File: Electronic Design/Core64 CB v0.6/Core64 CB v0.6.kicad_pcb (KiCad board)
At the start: 2 copper layers, 85 x 85 mm, 54 parts, among them J1 Digi-Key 77311-420-36LF-ND, J2 Digi-Key 77311-420-36LF-ND, U1 SI7210-B-01, U10 TS3A4751PWR, U11 SM353LT, U12 SM353LT, U13 SM353LT, U14 LTR-329ALS-01, U2 SI7210-B-02, U3 SI7210-B-03, U4 SI7210-B-04, U5 BH1730FVC, U6 BH1730FVC, U7 LTR-303ALS-01, U8 SM353LT, U9 TS3A4751PWR, X1 SFH11-NBPC-D03-ST-BK

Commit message: CB refine silkscreen, change center ALS BH1730 opening to drill hole and remove center solder pad, clean-up ref. des. numbers
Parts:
- J1, J2: value Digi-Key 77311-420-36LF-ND -> 929834-04-36-RK
- renumbered C7 to C6, C8 to C7, C9 to C8, R7 to R5, R5 to R6, U11 to U10, U12 to U11, U13 to U12, U9 to U13, U10 to U14, U14 to U8, U8 to U9
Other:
- outline, holes or cut-outs redrawn
- board text added: "*5V0 *GND XT3,7 XT2,6 XT1,5 XT0,4 XB0 XB1 XB2 XB3 XB4 XB5 XB6 XB7 P1G1 P2G2 CP3 CP4 *+BAT *5USB"
- board text added: "*LSIG *USR1 YL0 YL1 YL2 YL3 YL4,6 YL5,7 SEN2 SEN1 SCL SDA 3V3 GNDD CP8 CP7 CP6 CP5 *USR2 *USR3"
- board text added: "*Pass-through, not connected to Core Board"
- board text added: "5V0* GND* XT3,7 XT2,6 XT1,5 XT0,4 XB0 XB1 XB2 XB3 XB4 XB5 XB6 XB7 P1G1 P2G2 CP3 CP4 +BATT* 5VUSB*"
- board text added: "ANDY GEPPERT"
- board text added: "BOTTOM SIDE"
- board text added: "CORE BOARD (CB) PCB P/N: 122-001 V0.6 (2021-08-08)"
- board text added: "LSIG* USR1* YL0 YL1 YL2 YL3 YL4,6 YL5,7 SEN2 SEN1 SCL SDA 3V3 GNDD CP8 CP7 CP6 CP5 USR2* USR3*"
- board text added: "TOP SIDE"
- board text added: "WWW.MACHINEIDEAS.COM"
- board text removed: "5V0 GND XT3,7 XT2,6 XT1,5 XT0,4 XB0 XB1 XB2 XB3 XB4 XB5 XB6 XB7 P1G1 P2G2 CP3 CP4 +BATT 5VUSB"
- board text removed: "CORE BOARD V0.6 2021-06-07 ANDY GEPPERT WWW.MACHINEIDEAS.COM"
- board text removed: "LSIG USR1 YL0 YL1 YL2 YL3 YL4,6 YL5,7 SEN2 SEN1 SCL SDA 3V3 GNDD CP8 CP7 CP6 CP5 USR2 USR3"

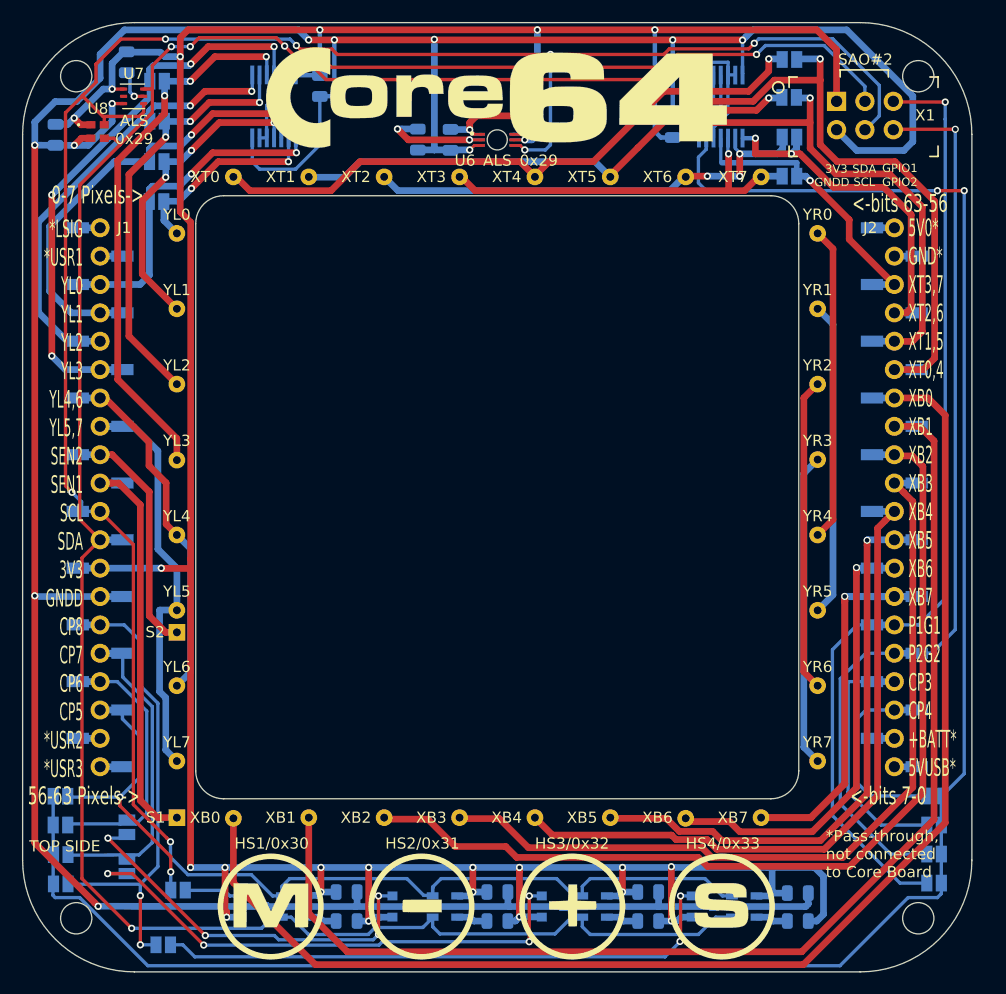
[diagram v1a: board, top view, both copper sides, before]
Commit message: Core Board V0.6 remove bottom ALS, add new top ALS+PROX option
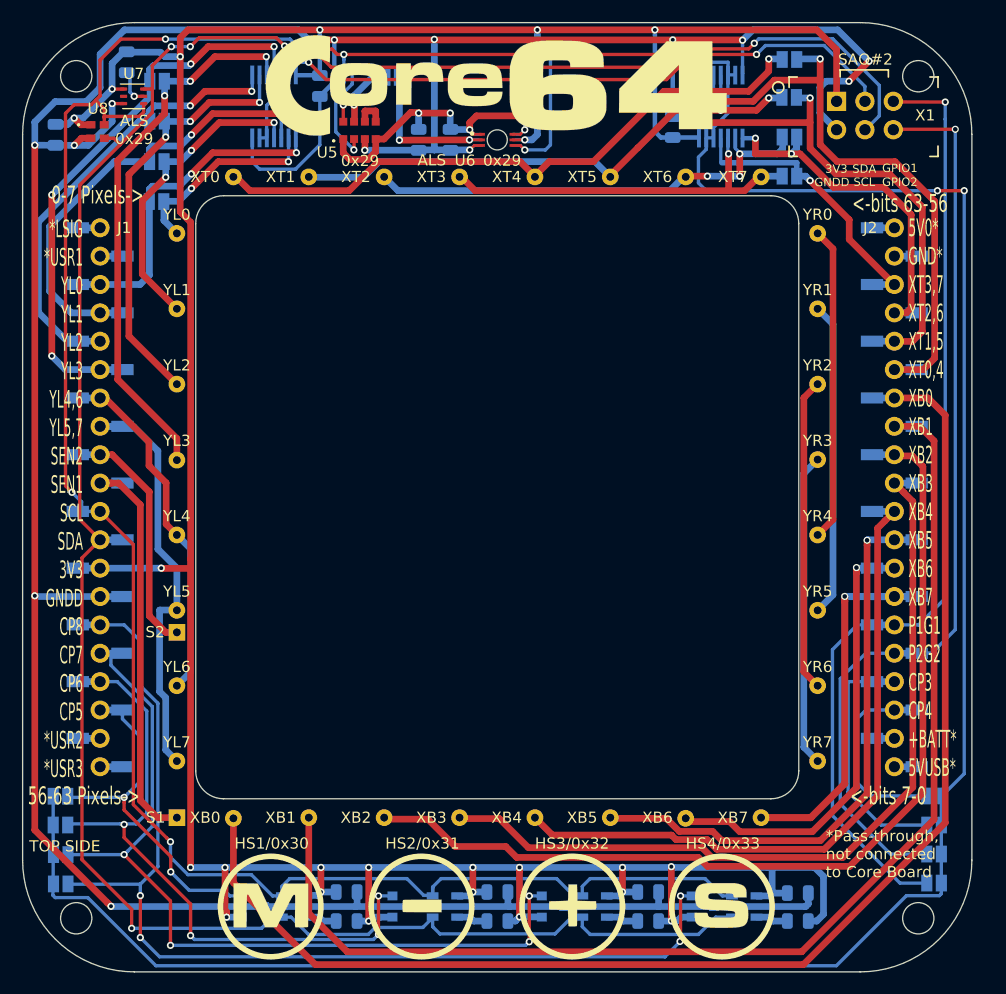
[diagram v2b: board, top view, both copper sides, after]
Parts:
- removed JP21, JP22, JP23, JP24: SolderJumper_2_Open, Jumper:SolderJumper-2_P1.3mm_Open_Pad1.0x1.5mm
- removed R6: 0, Resistor_SMD:R_0805_2012Metric
- added C9: 10uF, Capacitor_SMD:C_0805_2012Metric, B.Cu at (-7.04, -32.0)
- added JP17: SolderJumper_2_Open, Jumper:SolderJumper-2_P1.3mm_Open_Pad1.0x1.5mm, B.Cu at (-9.41, -37.6)
- U5: value BH1730FVC -> RPR-0521RS; footprint ALS_BH1730:BH1730-backside -> Rohm_RPR-0521RS:RPR0521RS; moved to F.Cu
- moved U5 12.4 mm to (-12.3, -32.9), turned to 0 degrees
- moved L1 1.09 mm to (1.79, -36.9)
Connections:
- U10 pad 2: Net-(JP22-Pad2) -> PLANE_6
- U11 pad 2: Net-(JP23-Pad2) -> PLANE_7
- U12 pad 2: Net-(JP24-Pad2) -> PLANE_8
- U5 pad 2: ALS_INT -> I2C_CLOCK
- U5 pad 4: I2C_CLOCK -> 3V3_800mA
- U5 pad 5: 3V3_800mA -> Net-(U5-Pad5)
- U5 pad 6: I2C_DATA -> Net-(U5-Pad5)
- U6 pad 2: ALS_INT -> Net-(JP17-Pad2)
- U9 pad 2: Net-(JP21-Pad2) -> PLANE_5
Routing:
- net PLANE_8: track 44.3 -> 96.9 mm, vias 2 -> 4
- net Net-(JP24-Pad2): track 51.7 -> 0.00 mm, vias 2 -> 0
- net Net-(JP23-Pad2): track 47.5 -> 0.00 mm, vias 4 -> 0
- net PLANE_7: track 30.5 -> 76.0 mm, vias 0 -> 4
- net Net-(JP22-Pad2): track 34.7 -> 0.00 mm, vias 4 -> 0
- net PLANE_6: track 24.0 -> 58.3 mm, vias 0 -> 4
- net 3V3_800mA: track 322.4 -> 338.8 mm, vias 25 -> 27
- net Net-(JP17-Pad2): track 0.00 -> 14.1 mm, vias 0 -> 2
- net I2C_CLOCK: track 234.1 -> 244.8 mm, vias 7 -> 9
- net PLANE_5: track 26.2 -> 31.8 mm
- net I2C_DATA: track 224.1 -> 229.3 mm, vias 7 -> 9
- net Net-(JP21-Pad2): track 5.21 -> 0.00 mm
- net ALS_INT: track 10.9 -> 5.82 mm, vias 2 -> 1
- net Net-(U5-Pad5): track 0.00 -> 2.88 mm
- net GNDD: track 306.7 -> 304.3 mm, vias 11 -> 14

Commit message: CB V0.6 added ALS and PROX, removed bottom ALS, complete BOM, PNP, and Gerbers for fabrication
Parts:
- U1: value SI7210-B-01 -> SI7210-B-00-IV
- U10, U11, U12, U9: value SM353LT -> TCS40DPR,LF
- U2: value SI7210-B-02 -> SI7210-B-02-IV
- U3: value SI7210-B-03 -> SI7210-B-03-IV
- U4: value SI7210-B-04 -> SI7210-B-04-IV
- renumbered C9 to C6, C6 to C7, C7 to C8, C8 to C9
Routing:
- net 3V3_800mA: track 338.8 -> 336.5 mm
- net I2C_CLOCK: track 244.8 -> 243.5 mm
- net GNDD: track 304.3 -> 303.1 mm
- net I2C_DATA: track 229.3 -> 228.0 mm
- net Net-(JP17-Pad2): track 14.1 -> 13.0 mm
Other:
- outline, holes or cut-outs redrawn
- board text added: "0x38"
- board text added: "CORE BOARD (CB) PCB P/N: 122-001 V0.6 (2021-10-14)"
- board text removed: "CORE BOARD (CB) PCB P/N: 122-001 V0.6 (2021-08-08)"
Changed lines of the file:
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@@
   (general
     (thickness 1.6)
-    (drawings 61)
-    (tracks 1002)
+    (drawings 60)
+    (tracks 992)
     (zones 0)
     (modules 51)
@@
       (drillshape 0)
       (scaleselection 1)
-      (outputdirectory "Core64_CB_V0.5_Gerbers/"))
+      (outputdirectory "Core64_CB_V0.6_Gerbers/"))
   )
   (net 0 "")
@@
   (module ALS_BH1730:REG_BD00IC0WHFV-GTR (layer F.Cu)
     (at 0 -32)
+    (attr smd)
     (fp_text reference U6 (at -2.885 1.85) (layer F.SilkS)
       (effects (font (size 1 1) (thickness 0.15)))
@@
   (module Core_Memory_8x8_Array:Core64-M_-_+_S_Buttons (layer F.Cu)
     (at -0.985 36.65)
+    (attr smd)
     (fp_text reference L2 (at 0 24.7) (layer F.SilkS) hide
       (effects (font (size 1.524 1.524) (thickness 0.3)))
@@
   (module Core_Memory_8x8_Array:Core64_Logo_9mm_tall (layer F.Cu)
     (at 1.79 -36.9)
+    (attr smd)
     (fp_text reference L1 (at 0 -12.25) (layer F.SilkS) hide
       (effects (font (size 1.524 1.524) (thickness 0.3)))
@@
       (effects (font (size 1 1) (thickness 0.15)) (justify mirror))
     )
-    (fp_text value SI7210-B-01 (at 0 -2.9) (layer B.Fab)
+    (fp_text value SI7210-B-00-IV (at 0 -2.9) (layer B.Fab)
       (effects (font (size 1 1) (thickness 0.15)) (justify mirror))
     )
@@
       (effects (font (size 1 1) (thickness 0.15)) (justify mirror))
     )
-    (fp_text value SI7210-B-02 (at 0 -2.9) (layer B.Fab)
+    (fp_text value SI7210-B-02-IV (at 0 -2.9) (layer B.Fab)
       (effects (font (size 1 1) (thickness 0.15)) (justify mirror))
     )
@@
       (effects (font (size 1 1) (thickness 0.15)) (justify mirror))
     )
-    (fp_text value SI7210-B-03 (at 0 -2.9) (layer B.Fab)
+    (fp_text value SI7210-B-03-IV (at 0 -2.9) (layer B.Fab)
       (effects (font (size 1 1) (thickness 0.15)) (justify mirror))
     )
@@
       (effects (font (size 1 1) (thickness 0.15)) (justify mirror))
     )
-    (fp_text value SI7210-B-04 (at 0 -2.9) (layer B.Fab)
+    (fp_text value SI7210-B-04-IV (at 0 -2.9) (layer B.Fab)
       (effects (font (size 1 1) (thickness 0.15)) (justify mirror))
     )
@@
     (tags capacitor)
     (attr smd)
-    (fp_text reference C6 (at 2.625 0.025 180) (layer B.SilkS)
+    (fp_text reference C7 (at 2.625 0.025 180) (layer B.SilkS)
       (effects (font (size 1 1) (thickness 0.15)) (justify mirror))
     )
@@
     (tags capacitor)
     (attr smd)
-    (fp_text reference C7 (at 2.525 -0.05 180) (layer B.SilkS)
+    (fp_text reference C8 (at 2.525 -0.05 180) (layer B.SilkS)
       (effects (font (size 1 1) (thickness 0.15)) (justify mirror))
     )
@@
     (tags capacitor)
     (attr smd)
-    (fp_text reference C8 (at -2.475 0 180) (layer B.SilkS)
+    (fp_text reference C9 (at -2.475 0 180) (layer B.SilkS)
       (effects (font (size 1 1) (thickness 0.15)) (justify mirror))
     )
@@
   (module TI_TS3A4751PWR:TS3A4751PWR (layer B.Cu)
     (at -19.985 -35 90)
+    (attr smd)
     (fp_text reference U13 (at -4.575 3.875 180) (layer B.SilkS)
       (effects (font (size 1 1) (thickness 0.15)) (justify mirror))
@@
   (module TI_TS3A4751PWR:TS3A4751PWR (layer B.Cu)
     (at 20.015 -34.9806 270)
+    (attr smd)
     (fp_text reference U14 (at -1.9694 4.3) (layer B.SilkS)
       (effects (font (size 1 1) (thickness 0.15)) (justify mirror))
@@
       (effects (font (size 1 1) (thickness 0.15)) (justify mirror))
     )
-    (fp_text value SM353LT (at 0 -2.5) (layer B.Fab)
+    (fp_text value TCS40DPR,LF (at 0 -2.5) (layer B.Fab)
       (effects (font (size 1 1) (thickness 0.15)) (justify mirror))
     )
@@
       (effects (font (size 1 1) (thickness 0.15)) (justify mirror))
     )
-    (fp_text value SM353LT (at 0 -2.5) (layer B.Fab)
+    (fp_text value TCS40DPR,LF (at 0 -2.5) (layer B.Fab)
       (effects (font (size 1 1) (thickness 0.15)) (justify mirror))
     )
@@
       (effects (font (size 1 1) (thickness 0.15)) (justify mirror))
     )
-    (fp_text value SM353LT (at 0 -2.5) (layer B.Fab)
+    (fp_text value TCS40DPR,LF (at 0 -2.5) (layer B.Fab)
       (effects (font (size 1 1) (thickness 0.15)) (justify mirror))
     )
@@
       (effects (font (size 1 1) (thickness 0.15)) (justify mirror))
     )
-    (fp_text value SM353LT (at 0 -2.5) (layer B.Fab)
+    (fp_text value TCS40DPR,LF (at 0 -2.5) (layer B.Fab)
       (effects (font (size 1 1) (thickness 0.15)) (justify mirror))
     )
@@
   (module LiteOn_LTR-329ALS:LTR-329ALS-01 (layer F.Cu)
     (at -35.785 -32.75)
+    (attr smd)
     (fp_text reference U8 (at 0.025 -2.05) (layer F.SilkS)
       (effects (font (size 1 1) (thickness 0.15)))
@@
     (tags capacitor)
     (attr smd)
-    (fp_text reference C9 (at 2.425 0.7 180) (layer B.SilkS)
+    (fp_text reference C6 (at 2.425 0.7 180) (layer B.SilkS)
       (effects (font (size 1 1) (thickness 0.15)) (justify mirror))
     )
@@
       (net 27 I2C_DATA))
   )
-  (gr_text 0x29 (at -12.285 -30.125) (layer F.SilkS)
+  (gr_text 0x38 (at -12.285 -30.125) (layer F.SilkS)
     (effects (font (size 1 1) (thickness 0.16)))
   )
@@
     (effects (font (size 1 1) (thickness 0.16)))
   )
-  (gr_circle (center 0 -32) (end 0.9 -32) (layer Edge.Cuts) (width 0.05))
   (gr_text "ANDY GEPPERT" (at 23.75 -41.5) (layer B.SilkS)
     (effects (font (size 1 1) (thickness 0.15)) (justify left mirror))
@@
     (effects (font (size 1 1) (thickness 0.15)) (justify left mirror))
   )
-  (gr_text "CORE BOARD (CB)     PCB P/N: 122-001     V0.6     (2021-08-08)" (at 0 41.5) (layer B.SilkS)
+  (gr_text "CORE BOARD (CB)     PCB P/N: 122-001     V0.6     (2021-10-14)" (at 0 41.5) (layer B.SilkS)
     (effects (font (size 1 1) (thickness 0.15)) (justify mirror))
   )
@@
   (via (at -5.635 -41) (size 0.65) (drill 0.35) (layers F.Cu B.Cu) (net 21))
   (via (at -2.465 -31.1) (size 0.65) (drill 0.35) (layers F.Cu B.Cu) (net 21))
-  (segment (start -2.065 -31.5) (end -1.375 -31.5) (width 0.25) (layer B.Cu) (net 21))
-  (segment (start -2.465 -31.1) (end -2.065 -31.5) (width 0.25) (layer B.Cu) (net 21))
   (segment (start -4.385 -31.1) (end -2.465 -31.1) (width 0.6) (layer B.Cu) (net 21))
   (segment (start -5.635 -41) (end -5.635 -31.1) (width 0.6) (layer B.Cu) (net 21))
@@
   (segment (start 3.59 -41.85) (end -27.685 -41.85) (width 0.6) (layer F.Cu) (net 26))
   (via (at 3.59 -41.85) (size 0.65) (drill 0.35) (layers F.Cu B.Cu) (net 26))
-  (segment (start 2.515 -32) (end 1.375 -32) (width 0.25) (layer B.Cu) (net 26))
   (segment (start 2.515 -32) (end 1.375 -32) (width 0.25) (layer F.Cu) (net 26))
   (via (at 2.465 -32) (size 0.65) (drill 0.35) (layers F.Cu B.Cu) (net 26))
@@
   (via (at 3.59 -34.15) (size 0.65) (drill 0.35) (layers F.Cu B.Cu) (net 26))
   (via (at -2.465 -32.9) (size 0.65) (drill 0.35) (layers F.Cu B.Cu) (net 26))
-  (segment (start -2.065 -32.5) (end -1.437001 -32.5) (width 0.25) (layer B.Cu) (net 26))
-  (segment (start -2.465 -32.9) (end -2.065 -32.5) (width 0.25) (layer B.Cu) (net 26))
   (segment (start -2.465 -33.545) (end -2.465 -32.9) (width 0.6) (layer F.Cu) (net 26))
   (segment (start -1.86 -34.15) (end -2.465 -33.545) (width 0.6) (layer F.Cu) (net 26))
@@
   (segment (start 2.465 -32.9) (end 2.065 -32.5) (width 0.25) (layer F.Cu) (net 27))
   (segment (start 2.065 -32.5) (end 1.375 -32.5) (width 0.25) (layer F.Cu) (net 27))
-  (segment (start 2.057 -32.508) (end 1.3716 -32.508) (width 0.25) (layer B.Cu) (net 27))
-  (segment (start 2.465 -32.9) (end 2.065 -32.5) (width 0.25) (layer B.Cu) (net 27))
   (segment (start -19.285 37.6) (end -18.455 37.6) (width 0.3) (layer B.Cu) (net 27))
   (segment (start -10.923961 38.522999) (end -6.657999 38.522999) (width 0.3) (layer B.Cu) (net 27))
@@
   (segment (start 2.065 -31.5) (end 1.375 -31.5) (width 0.25) (layer F.Cu) (net 28))
   (segment (start 2.465 -31.1) (end 2.065 -31.5) (width 0.25) (layer F.Cu) (net 28))
-  (segment (start 2.065 -31.5) (end 2.465 -31.1) (width 0.25) (layer B.Cu) (net 28))
-  (segment (start 1.3716 -31.5) (end 2.065 -31.5) (width 0.25) (layer B.Cu) (net 28))
   (segment (start -29.26 31.309617) (end -29.26 30.849998) (width 0.3) (layer B.Cu) (net 28))
   (segment (start -35.56 1.27) (end -32.584999 4.245001) (width 0.3) (layer F.Cu) (net 28))
@@
   (segment (start -32.51 -35.9) (end -32.885 -36.275) (width 0.3) (layer B.Cu) (net 60))
   (via (at -2.485 -32) (size 0.65) (drill 0.35) (layers F.Cu B.Cu) (net 61))
-  (segment (start -2.485 -32) (end -1.36 -32) (width 0.25) (layer B.Cu) (net 61))
   (segment (start -2.485 -32) (end -1.375 -32) (width 0.25) (layer F.Cu) (net 61))
   (segment (start -8.76 -31.975) (end -8.76 -31.975) (width 0.6) (layer F.Cu) (net 61))
